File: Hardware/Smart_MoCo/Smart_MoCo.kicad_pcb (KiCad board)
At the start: 2 copper layers, 33.5 x 53.1 mm, 43 parts, among them J1 Conn_01x04, J2 Conn_01x05, U1 STM32F042F6Px, U2 VNH5019A-E, U3 ATA6561

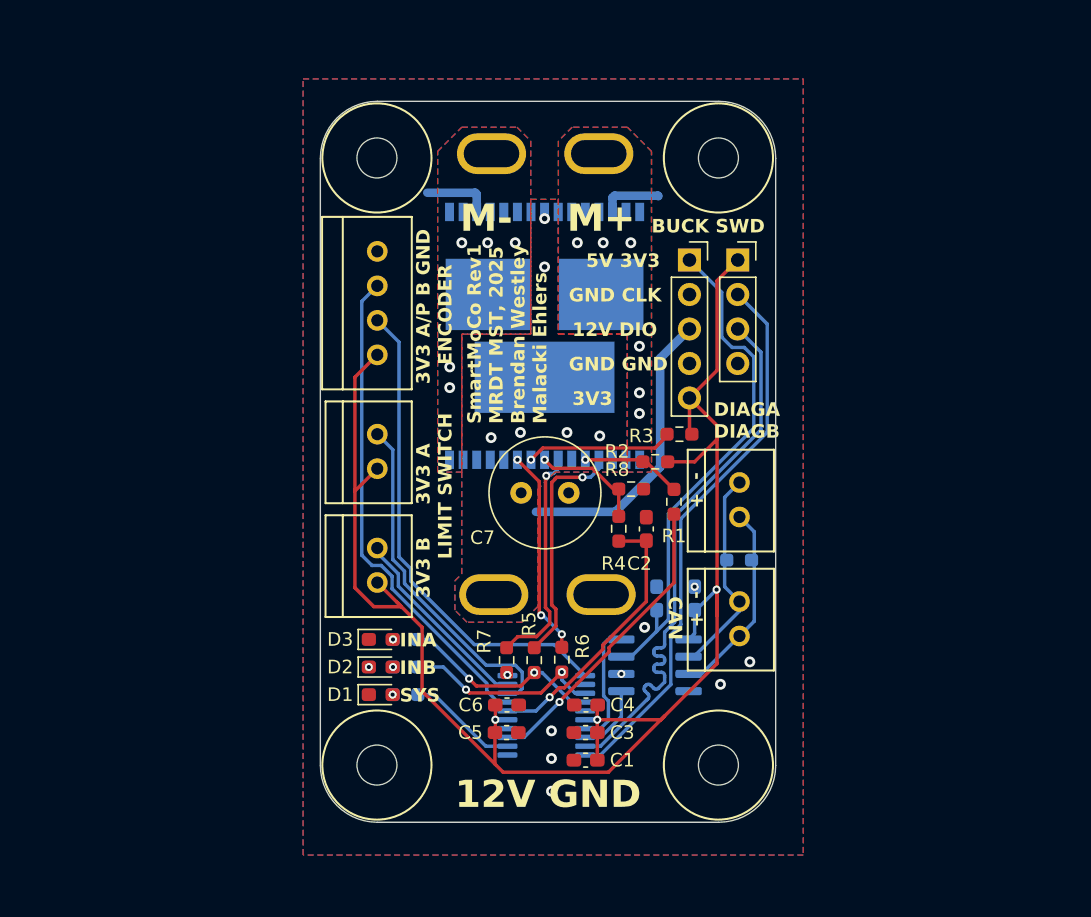
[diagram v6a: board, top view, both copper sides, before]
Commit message: Change power connectors, increase layer count to 4, and reroute
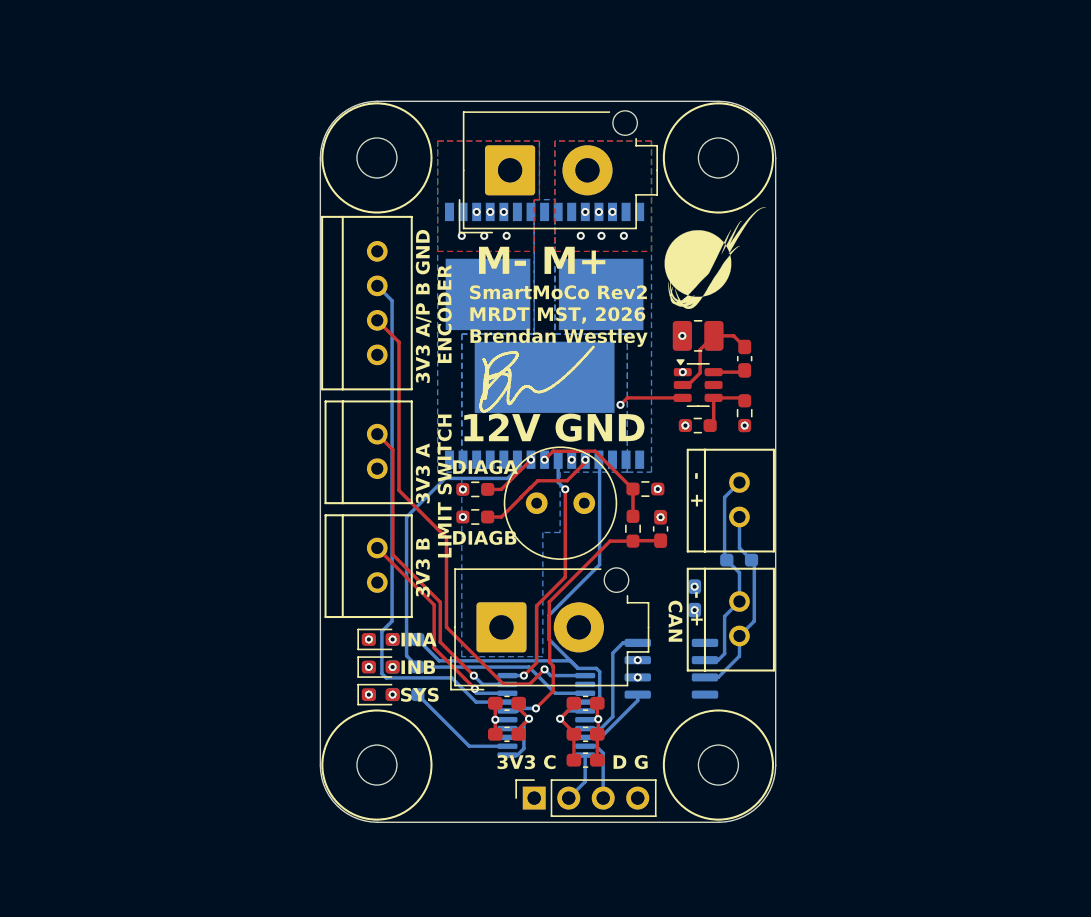
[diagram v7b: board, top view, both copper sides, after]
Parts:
- removed C9: 100nF, Capacitor_SMD:C_0603_1608Metric_Pad1.08x0.95mm_HandSolder
- removed Conn6, Conn7: AndersonPP, Local Libraries:Square_Anderson_2_V_Side_By_Side_No_Silkscreen
- removed the G*** at (154.2, 89.9)
- removed R1, R7: 1k, Resistor_SMD:R_0603_1608Metric_Pad0.98x0.95mm_HandSolder
- added C10: 100nF, Capacitor_SMD:C_0603_1608Metric_Pad1.08x0.95mm_HandSolder, F.Cu at (167.1, 75.2)
- added J4: Conn_01x02, Connector_Molex:Molex_Mega-Fit_76829-0102_2x01_P5.70mm_Vertical, F.Cu at (149.9, 61.3)
- added L2: 3.3uH, Inductor_SMD:L_1008_2520Metric_Pad1.43x2.20mm_HandSolder, F.Cu at (163.7, 73.5)
- added U4: AP62200WU, Package_TO_SOT_SMD:TSOT-23-6, F.Cu at (163.7, 77.2)
- G***, REF**: moved to F.Cu
- J2: value Conn_01x05 -> Conn_01x02; footprint Connector_PinSocket_2.54mm:PinSocket_1x05_P2.54mm_Vertical -> Connector_Molex:Molex_Mega-Fit_76829-0102_2x01_P5.70mm_Vertical
- R5: value 1k -> 31.6k
- R6: value 1k -> 10k
- U3: value ATA6561 -> SN65HVD232
- moved J1 42.4 mm to (151.6, 107.6), turned to 90 degrees
- moved J2 30.4 mm to (149.2, 95.0), turned to 90 degrees
- moved G*** 27.6 mm to (165.0, 67.8), turned to 0 degrees
- moved R5 23.9 mm to (167.1, 79.2), turned to 90 degrees
- moved R6 19.9 mm to (163.7, 80.1), turned to 180 degrees
- moved R3 15.6 mm to (147.3, 84.8), turned to 0 degrees
- moved REF** 13.9 mm to (151.6, 76.7), turned to 0 degrees
- moved R2 13.9 mm to (147.3, 86.9), turned to 0 degrees
- moved Conn4 8.38 mm to (140.1, 91.7)
- moved Conn5 8.38 mm to (140.1, 83.3)
- moved C7 1.37 mm to (151.8, 85.9)
- moved U3 1.23 mm to (161.7, 98.0)
- moved C2 1.05 mm to (160.9, 87.7)
- moved R4 1.05 mm to (158.9, 87.7)
- moved R8 1.05 mm to (159.8, 84.8)
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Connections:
- J2 pad 1: +5V -> +12V
- R5 pad 1: Net-(U2-INA) -> +3V3
- R5 pad 2: IN_A -> Net-(U4-FB)
- R6 pad 1: Net-(U2-INB) -> Net-(U4-FB)
- R6 pad 2: IN_B -> GND
- U1 pad 3: DIAG_A -> unconnected-(U1-PF1-Pad3)
- U2 pad 10: Net-(U2-INB) -> IN_B
- U2 pad 4: Net-(U2-INA) -> IN_A
- U2 pad 7: Net-(U2-PWM) -> PWM
- U3 pad 3: +5V -> +3V3
- U3 pad 5: +3V3 -> unconnected-(U3-NC-Pad5)
- U3 pad 8: GND -> unconnected-(U3-NC-Pad8)
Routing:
- net +3V3: track 121.9 -> 8.15 mm, vias 3 -> 8
- net SWCLK: track 41.0 -> 3.67 mm
- net +5V: track 37.1 -> 0.00 mm
- net SWDIO: track 40.9 -> 4.85 mm
- net DIAG_A: track 22.1 -> 0.00 mm, vias 1 -> 0
- net IN_A: track 15.1 -> 35.3 mm, vias 2 -> 0
- net IN_B: track 14.7 -> 34.8 mm, vias 2 -> 0
- net PWM: track 0.00 -> 18.6 mm, vias 1 -> 2
- net Net-(U2-INA): track 17.5 -> 0.00 mm, vias 1 -> 0
- net +12V: track 21.6 -> 4.80 mm, vias 6 -> 1
- net Net-(U2-PWM): track 16.7 -> 0.00 mm, vias 1 -> 0
- net Net-(U2-INB): track 15.2 -> 0.00 mm, vias 3 -> 0
- net LIM_A: track 25.6 -> 16.0 mm, vias 0 -> 1
- net LIM_B: track 14.1 -> 23.5 mm, vias 0 -> 1
- net Net-(U4-SW): track 0.00 -> 7.40 mm
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- added copper zone on In2.Cu, net +12V
- added copper zone on In2.Cu, net +3V3
- added copper zone on In2.Cu, net /OUTA
- added copper zone on In2.Cu, net /OUTB
- added copper zone on In1.Cu, net GND
- removed copper zone on F.Cu, net +12V
- removed copper zone on B.Cu, net GND
- removed copper zone on F.Cu, net GND
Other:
- copper layers 2 -> 4
- board text added: "3V3 C"
- board text added: "D G"
- board text added: "DIAGA"
- board text added: "DIAGB"
- board text added: "M- M+"
- board text added: "SmartMoCo Rev2 MRDT MST, 2026 Brendan Westley"
- board text removed: "12V DIO"
- board text removed: "3V3"
- board text removed: "5V 3V3"
- board text removed: "BUCK SWD"
- board text removed: "DIAGA DIAGB"
- board text removed: "GND CLK"
- board text removed: "GND GND"
- board text removed: "M+"
- board text removed: "M-"
- board text removed: "SmartMoCo Rev1 MRDT MST, 2025 Brendan Westley Malacki Ehlers"

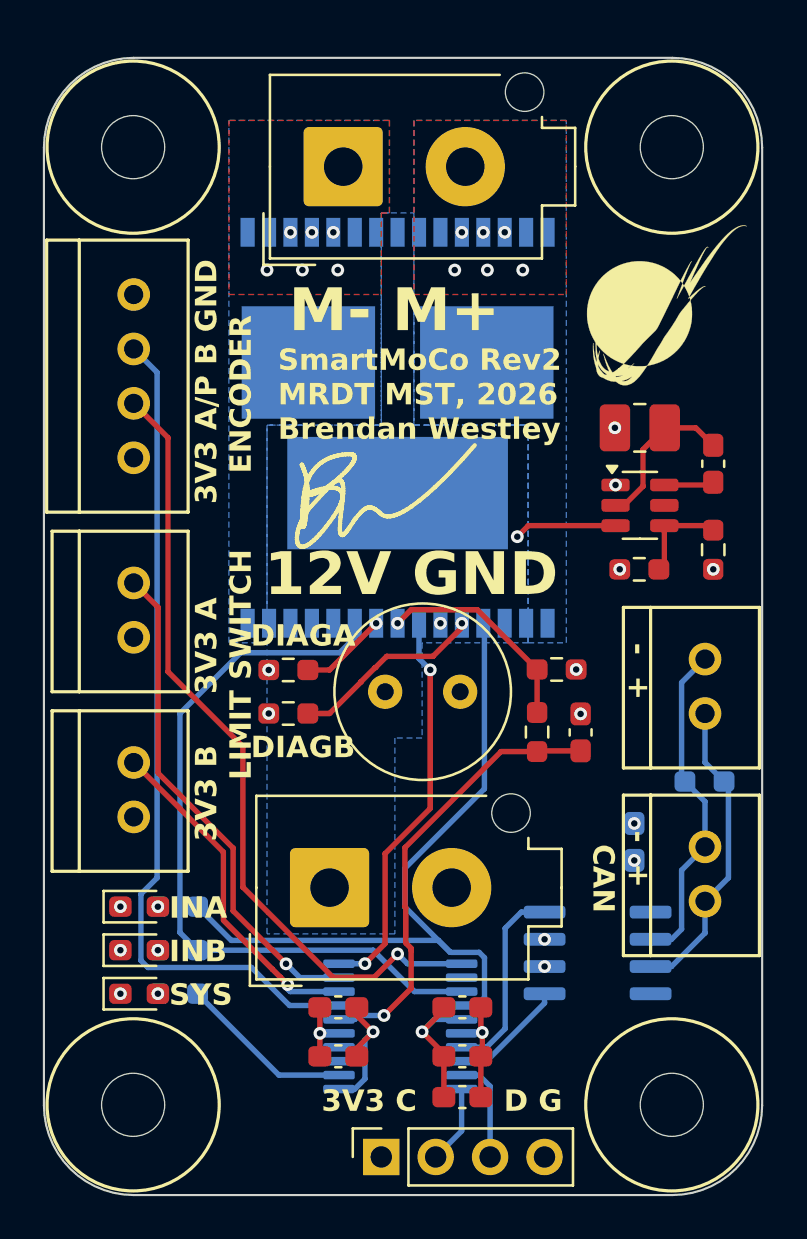
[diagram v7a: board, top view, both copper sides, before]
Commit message: Change power connectors again
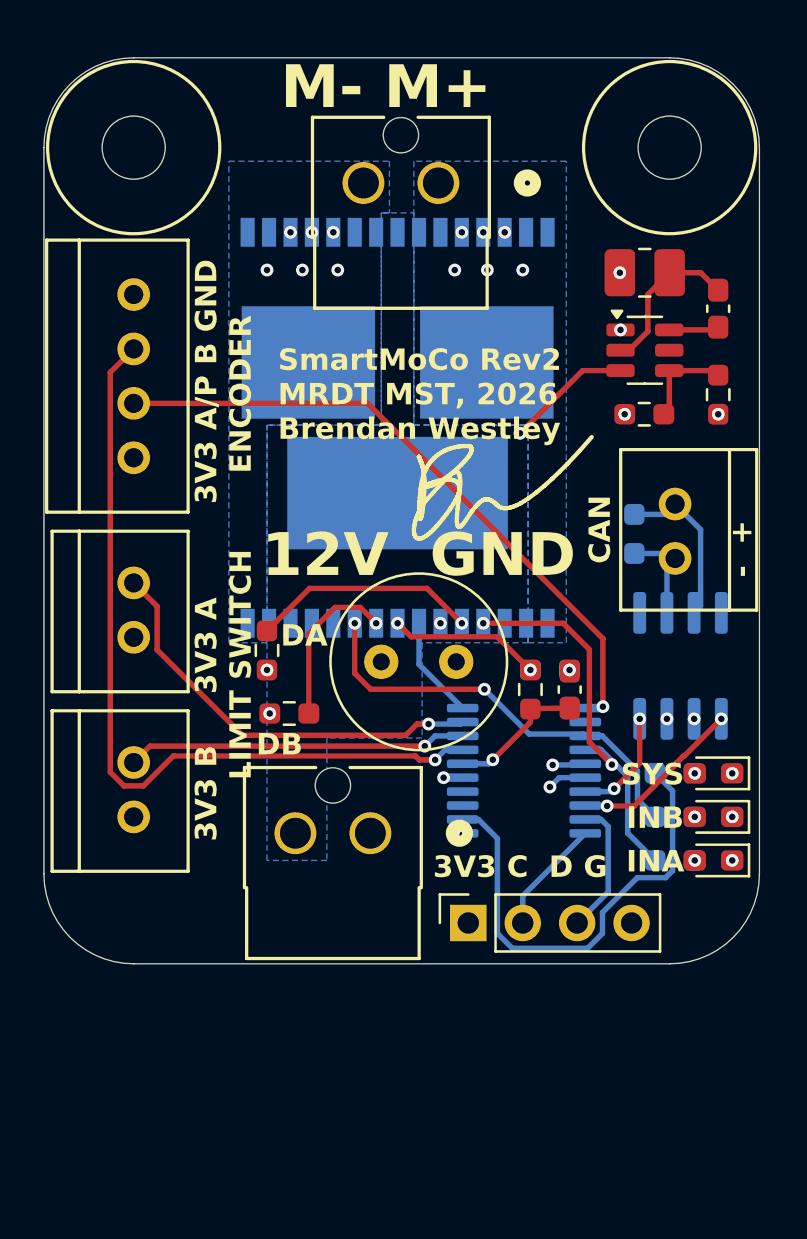
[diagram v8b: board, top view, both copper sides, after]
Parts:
- removed C1, C3, C8: 100nF, Capacitor_SMD:C_0603_1608Metric_Pad1.08x0.95mm_HandSolder
- removed C4: 4.7uF, Capacitor_SMD:C_0603_1608Metric_Pad1.08x0.95mm_HandSolder
- removed C5: 10nF, Capacitor_SMD:C_0603_1608Metric_Pad1.08x0.95mm_HandSolder
- removed C6: 1uF, Capacitor_SMD:C_0603_1608Metric_Pad1.08x0.95mm_HandSolder
- removed Conn2: Molex_SL_02, MRDT_Connectors:MOLEX_SL_02_Vertical
- removed H3, H4: MountingHole, MRDT_Drill_Holes:4_40_Hole
- G***, R8: moved to B.Cu
- J2, J4: value Conn_01x02 -> 1722861102; footprint Connector_Molex:Molex_Mega-Fit_76829-0102_2x01_P5.70mm_Vertical -> MRDT_Connectors:CONN_SD-172286-1000_02_MOL
- moved H2 44.7 mm to (140.1, 60.5)
- moved D1 28.7 mm to (167.1, 89.7), turned to 180 degrees
- moved D2 27.5 mm to (167.1, 91.7), turned to 180 degrees
- moved D3 26.9 mm to (167.1, 93.7), turned to 180 degrees
- moved R10 25.4 mm to (165.3, 89.7), turned to 0 degrees
- moved R11 24.0 mm to (165.3, 91.7), turned to 0 degrees
- moved R12 23.3 mm to (165.3, 93.7), turned to 0 degrees
- moved U3 13.9 mm to (165.6, 84.6), turned to 90 degrees
- moved U1 13.3 mm to (158.3, 89.5)
- moved R9 12.0 mm to (163.4, 78.5), turned to -90 degrees
- moved J1 11.7 mm to (155.7, 96.6)
- moved Conn1 9.88 mm to (165.4, 77.1), turned to -90 degrees
- moved L2 7.24 mm to (163.9, 66.3)
- moved R5 7.24 mm to (167.4, 72.0)
- moved U4 7.24 mm to (163.9, 69.9)
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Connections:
- J2 pad 1: +12V -> GND
- J2 pad 2: GND -> +12V
- J4 pad 1: /OUTB -> /OUTA
- J4 pad 2: /OUTA -> /OUTB
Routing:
- net IN_A: track 35.3 -> 18.2 mm, vias 0 -> 2
- net IN_B: track 34.8 -> 19.9 mm, vias 0 -> 2
- net CS: track 20.7 -> 6.41 mm
- net PWM: track 18.6 -> 4.80 mm, vias 2 -> 0
- net LED_STATUS: track 8.18 -> 21.8 mm
- net GND: track 13.8 -> 0.83 mm, vias 18 -> 16
- net CANL: track 15.6 -> 4.55 mm
- net ENC_A/PWM: track 37.3 -> 30.5 mm
- net CANH: track 14.3 -> 7.80 mm
- net +3V3: track 8.15 -> 2.72 mm, vias 8 -> 7
- net CAN_RX: track 9.23 -> 5.16 mm, vias 0 -> 2
- net LIM_B: track 23.5 -> 19.7 mm
- net Net-(U2-EN/DIAGB): track 4.09 -> 7.69 mm
- net Net-(U2-CS): track 9.94 -> 7.10 mm, vias 1 -> 2
- net CAN_TX: track 5.43 -> 8.02 mm, vias 0 -> 2
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- removed copper zone on F.Cu, net /OUTA
- removed copper zone on F.Cu, net /OUTB
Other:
- board size 33.5 x 53.1 mm -> 33.4 x 42.3 mm
- board text added: "3V3 C D G"
- board text added: "DA"
- board text added: "DB"
- board text removed: "3V3 C"
- board text removed: "D G"
- board text removed: "DIAGA"
- board text removed: "DIAGB"
